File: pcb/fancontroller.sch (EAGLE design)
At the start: 109 parts, among them CN1 USB-MICROB-2TABS, Q1 AO3401, Q10 AO3401, Q11 AO3402, Q12 AO3402, Q13 AO3402, Q14 AO3402, Q15 AO3402, Q16 AO3402, Q17 AO3402, Q18 AO3402, Q2 AO3401, Q3 AO3401, Q4 AO3401, Q5 AO3401, Q6 AO3401, Q7 AO3401, Q8 AO3401, Q9 8M, U1 RT9193, U2 STM32F103-48LQFP

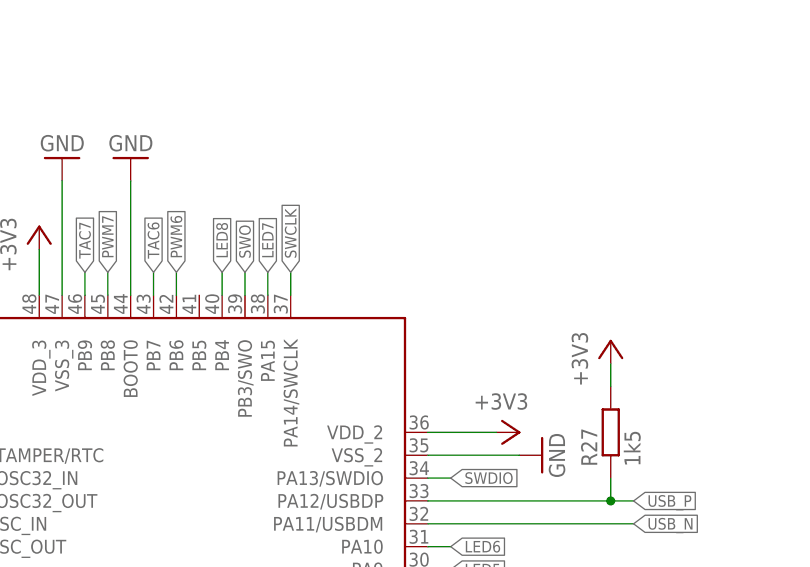
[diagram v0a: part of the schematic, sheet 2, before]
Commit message: pcb: Connect USB pull-up resistor to GPIO
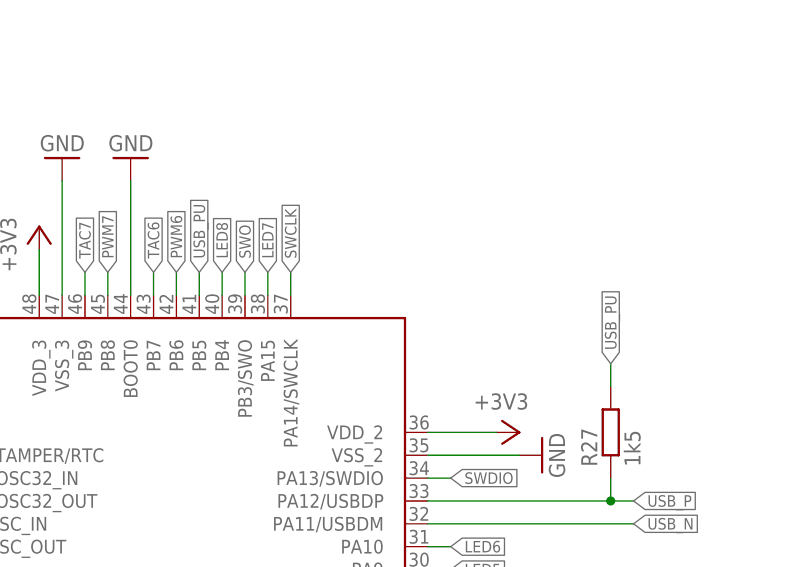
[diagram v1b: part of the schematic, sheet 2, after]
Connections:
- new net USB_PU: R27.2, U2.PB5
- net +3V3: no longer R27.2
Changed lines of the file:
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@@
 <?xml version="1.0" encoding="utf-8"?>
 <!DOCTYPE eagle SYSTEM "eagle.dtd">
-<eagle version="8.5.0">
+<eagle version="9.0.0">
 <drawing>
 <settings>
@@
 <setting verticaltext="up"/>
 </settings>
-<grid distance="0.1" unitdist="inch" unit="inch" style="dots" multiple="1" display="yes" altdistance="0.01" altunitdist="inch" altunit="inch"/>
+<grid distance="0.1" unitdist="inch" unit="inch" style="lines" multiple="1" display="no" altdistance="0.01" altunitdist="inch" altunit="inch"/>
 <layers>
 <layer number="1" name="Top" color="4" fill="1" visible="no" active="no"/>
@@
 <part name="+3V1" library="supply1" deviceset="+3V3" device=""/>
 <part name="R27" library="tuetuopay" deviceset="R" device="R0603" value="1k5"/>
-<part name="+3V2" library="supply1" deviceset="+3V3" device=""/>
 <part name="GND30" library="supply1" deviceset="GND" device=""/>
 <part name="R28" library="tuetuopay" deviceset="R" device="R0603" value="10k"/>
@@
 <instance part="+3V1" gate="G$1" x="220.98" y="114.3"/>
 <instance part="R27" gate="G$1" x="165.1" y="106.68" rot="R90"/>
-<instance part="+3V2" gate="G$1" x="165.1" y="116.84"/>
 </instances>
 <busses>
@@
 <pinref part="LED6" gate="G$1" pin="A"/>
 </segment>
-<segment>
-<pinref part="R27" gate="G$1" pin="2"/>
-<pinref part="+3V2" gate="G$1" pin="+3V3"/>
-<wire x1="165.1" y1="111.76" x2="165.1" y2="114.3" width="0.1524" layer="91"/>
-</segment>
 </net>
 <net name="SWDIO" class="0">
@@
 </segment>
 </net>
+<net name="USB_PU" class="0">
+<segment>
+<pinref part="U2" gate="G$1" pin="PB5"/>
+<wire x1="119.38" y1="121.92" x2="119.38" y2="124.46" width="0.1524" layer="91"/>
+<label x="119.38" y="124.46" size="1.27" layer="95" rot="R90" xref="yes"/>
+</segment>
+<segment>
+<pinref part="R27" gate="G$1" pin="2"/>
+<wire x1="165.1" y1="111.76" x2="165.1" y2="114.3" width="0.1524" layer="91"/>
+<label x="165.1" y="114.3" size="1.27" layer="95" rot="R90" xref="yes"/>
+</segment>
+</net>
